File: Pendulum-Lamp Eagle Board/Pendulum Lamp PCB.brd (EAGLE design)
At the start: 70.5 x 88.6 mm, 16 parts, among them IC1 LM324N, IC2 7805TV, IC3 LM324N, IC4 7805TV, X1 2514-

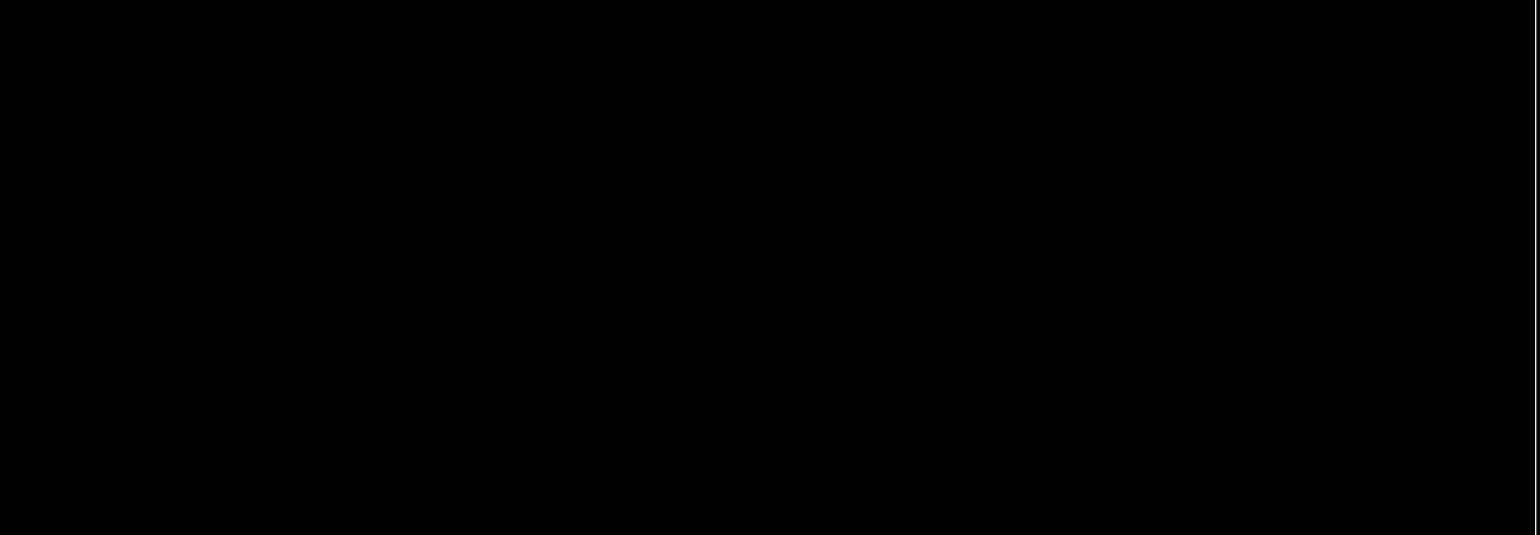
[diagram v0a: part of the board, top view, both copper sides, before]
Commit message: Sensor Array finished
Added sensor array in Eagle and DXF
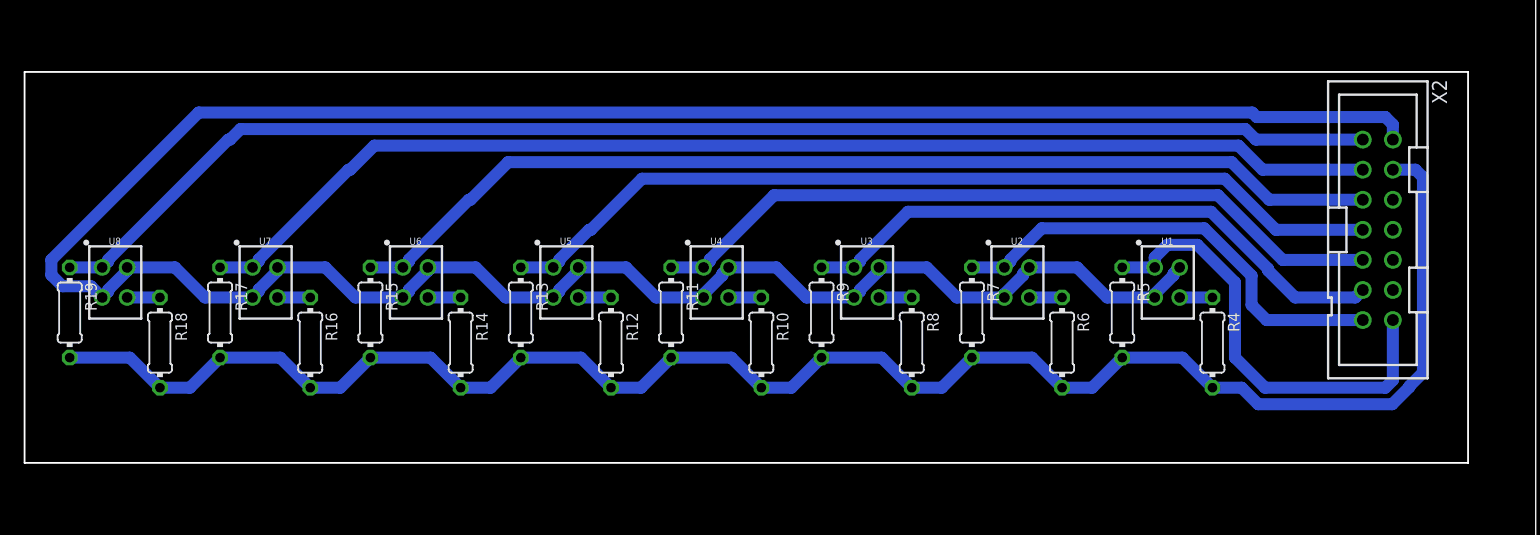
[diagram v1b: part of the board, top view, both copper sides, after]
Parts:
- added R10, R12, R14, R16, R18, R4, R6, R8: 330, rcl:0204/7
- added R11, R13, R15, R17, R19, R5, R7, R9: 10k, rcl:0204/7
- added U1, U2, U3, U4, U5, U6, U7, U8: QRD1114, SparkFun-Sensors:QRD1114
- added X2: 2514-, con-3m:PAK100/2500-14
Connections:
- new net GND_2: U1.2, U1.4, U2.2, U2.4, U3.2, U3.4, U4.2, U4.4, U5.2, U5.4, U6.2, U6.4, U7.2, U7.4, U8.2, U8.4, X2.2
- new net N$30: R4.1, U1.3
- new net N$31: R5.1, U1.1, X2.14
- new net N$34: R6.1, U2.3
- new net N$36: R7.1, U2.1, X2.13
- new net N$38: R8.1, U3.3
- new net N$40: R9.1, U3.1, X2.11
- new net N$42: R10.1, U4.3
- new net N$44: R11.1, U4.1, X2.9
- new net N$46: R12.1, U5.3
- new net N$48: R13.1, U5.1, X2.7
- new net N$50: R14.1, U6.3
- new net N$52: R15.1, U6.1, X2.5
- new net N$54: R16.1, U7.3
- new net N$56: R17.1, U7.1, X2.3
- new net N$58: R18.1, U8.3
- new net N$60: R19.1, U8.1, X2.1
- new net VCC_2: R10.2, R11.2, R12.2, R13.2, R14.2, R15.2, R16.2, R17.2, R18.2, R19.2, R4.2, R5.2, R6.2, R7.2, R8.2, R9.2, X2.4
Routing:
- net GND_2: track 0.00 -> 235.3 mm
- net VCC_2: track 0.00 -> 151.1 mm
- net N$60: track 0.00 -> 114.5 mm
- net N$56: track 0.00 -> 101.7 mm
- net N$52: track 0.00 -> 88.9 mm
- net N$48: track 0.00 -> 76.1 mm
- net N$44: track 0.00 -> 63.3 mm
- net N$40: track 0.00 -> 51.1 mm
- net N$36: track 0.00 -> 39.1 mm
- net N$31: track 0.00 -> 38.2 mm
- net N$34: track 0.00 -> 2.77 mm
- net N$50: track 0.00 -> 2.77 mm
- net N$46: track 0.00 -> 2.77 mm
- net N$42: track 0.00 -> 2.77 mm
- net N$58: track 0.00 -> 2.77 mm
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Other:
- board size 70.5 x 88.6 mm -> 198.1 x 88.6 mm
